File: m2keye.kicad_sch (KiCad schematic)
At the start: 17 parts

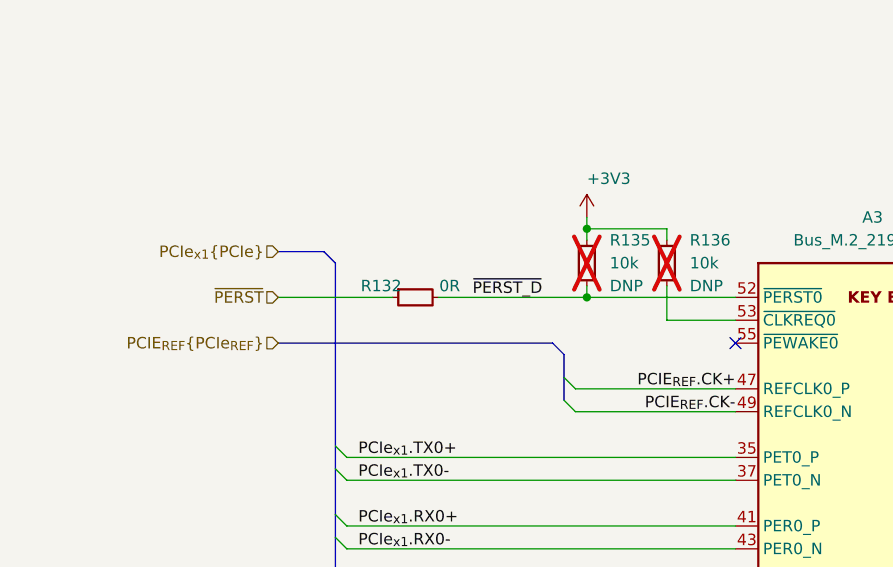
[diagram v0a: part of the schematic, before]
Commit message: [#58904] Change pinout of backplane connector. Connect CLKREQ from PCIe devices
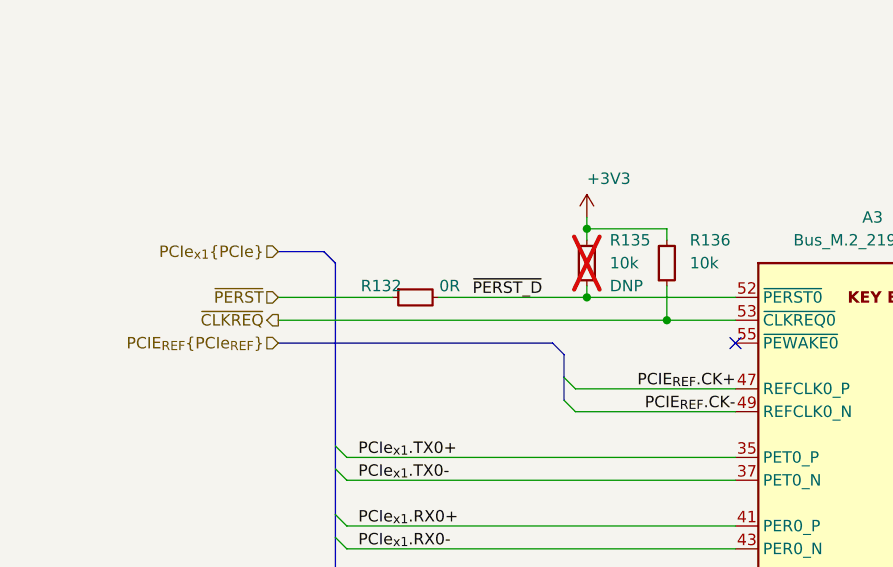
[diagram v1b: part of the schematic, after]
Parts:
- R136: DNP DNP -> (none); now fitted
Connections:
- net ~{CLKREQ}: now reaches A3.53 (~{CLKREQ0}), R136.1
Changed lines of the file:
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@@
   (junction (at 166.37 82.55) (diameter 0) (color 0 0 0 0)
+  )
+  (junction (at 175.26 85.09) (diameter 0) (color 0 0 0 0)
   )
   (junction (at 218.44 189.23) (diameter 0) (color 0 0 0 0)
@@
     (stroke (width 0) (type default))
   )
+  (wire (pts (xy 132.08 85.09) (xy 175.26 85.09))
+    (stroke (width 0) (type default))
+  )
   (bus (pts (xy 138.43 158.75) (xy 138.43 161.29))
     (stroke (width 0) (type default))
@@
   )
   (hierarchical_label "PCIe_{x1}{PCIe}" (shape input) (at 132.08 77.47 180) (fields_autoplaced)
+    (effects (font (size 1.27 1.27)) (justify right))
+  )
+  (hierarchical_label "~{CLKREQ}" (shape output) (at 132.08 85.09 180) (fields_autoplaced)
     (effects (font (size 1.27 1.27)) (justify right))
   )
@@
   )
   (symbol (lib_id "antmicroResistors0402:R_10k_0402") (at 175.26 81.28 90) (unit 1)
-    (in_bom yes) (on_board yes) (dnp yes) (fields_autoplaced)
+    (in_bom yes) (on_board yes) (dnp no) (fields_autoplaced)
     (property "Reference" "R136" (at 177.8 76.2 90)
       (effects (font (size 1.27 1.27) (thickness 0.15)) (justify right))
@@
       (effects (font (size 1.27 1.27)) (justify left bottom) hide)
     )
-    (property "DNP" "DNP" (at 177.8 81.28 90)
-      (effects (font (size 1.27 1.27)) (justify right))
-    )
     (pin "2")

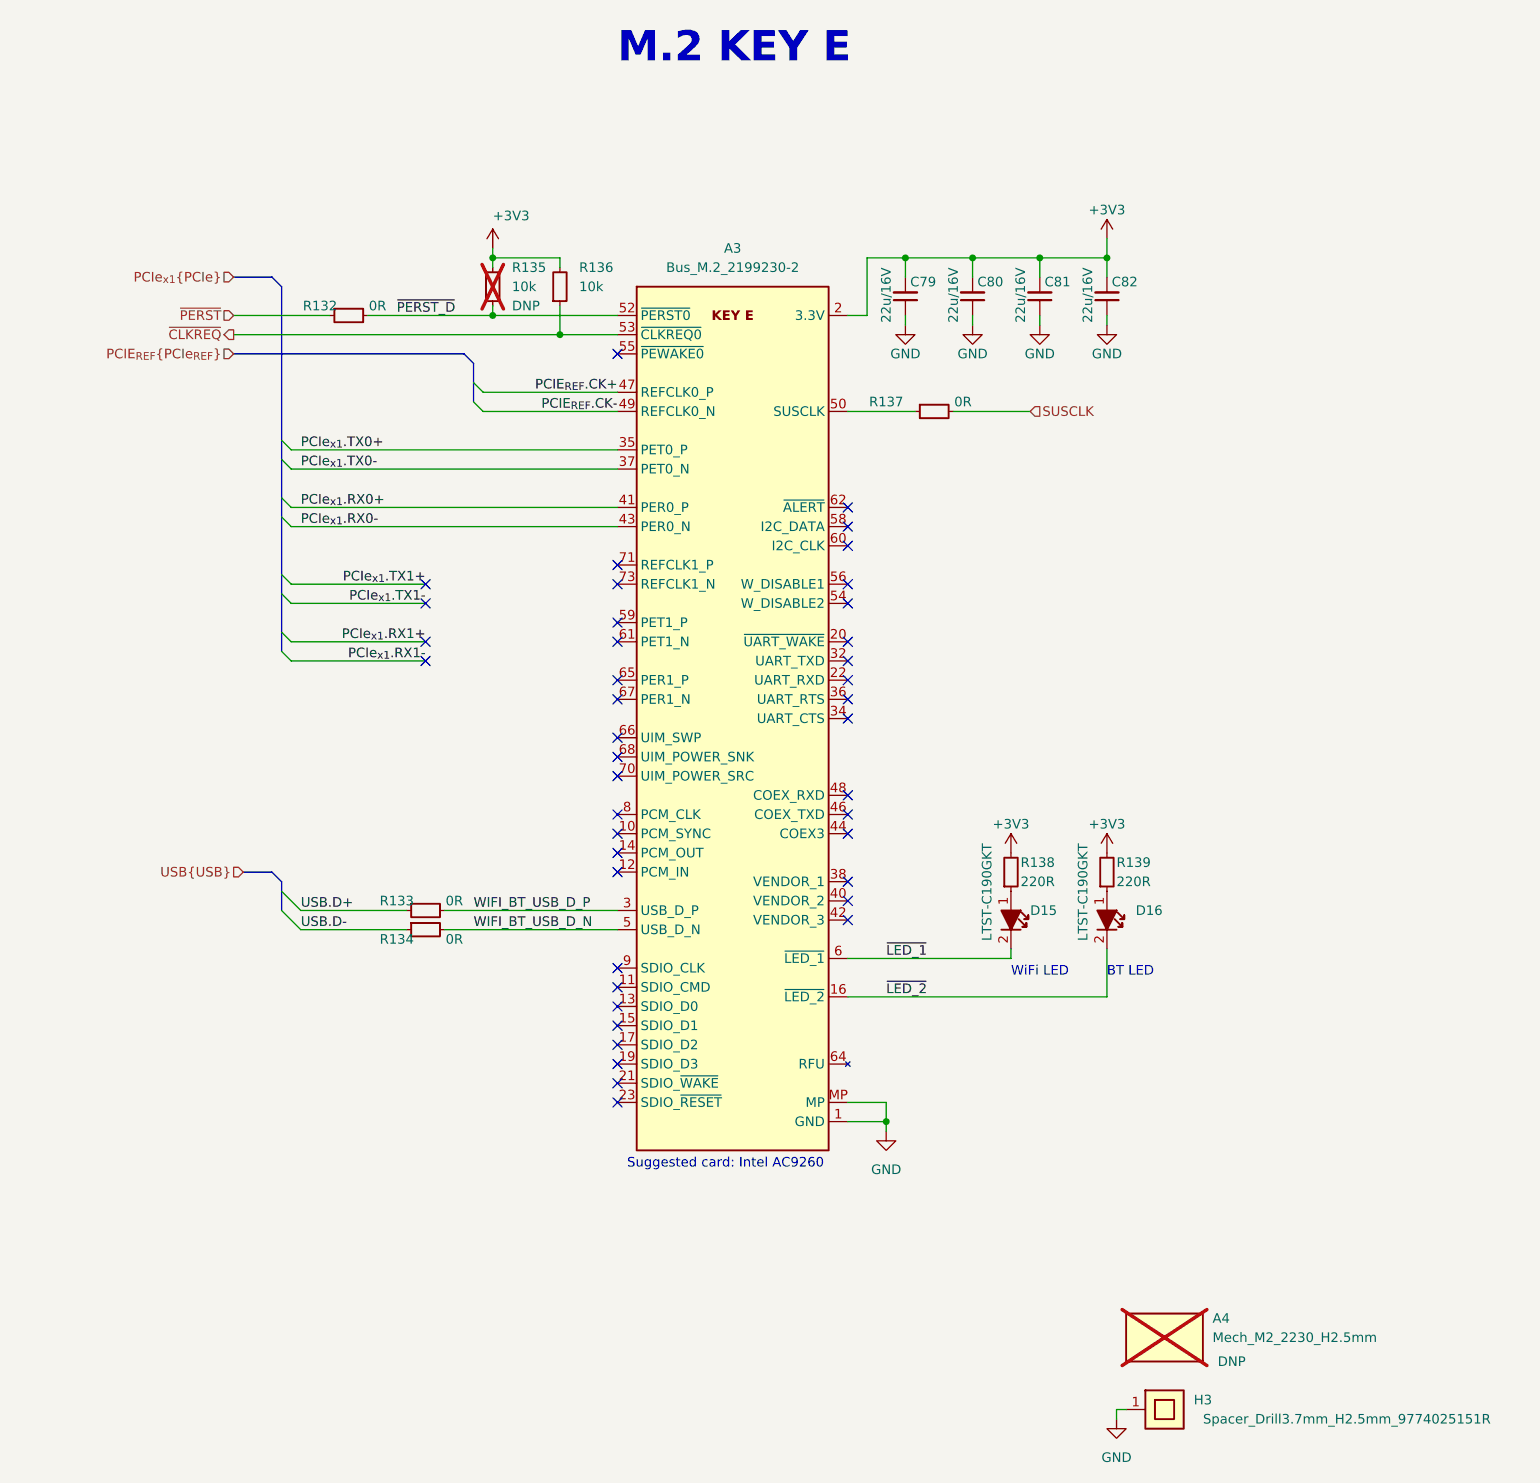
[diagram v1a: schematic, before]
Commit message: Update components from the library
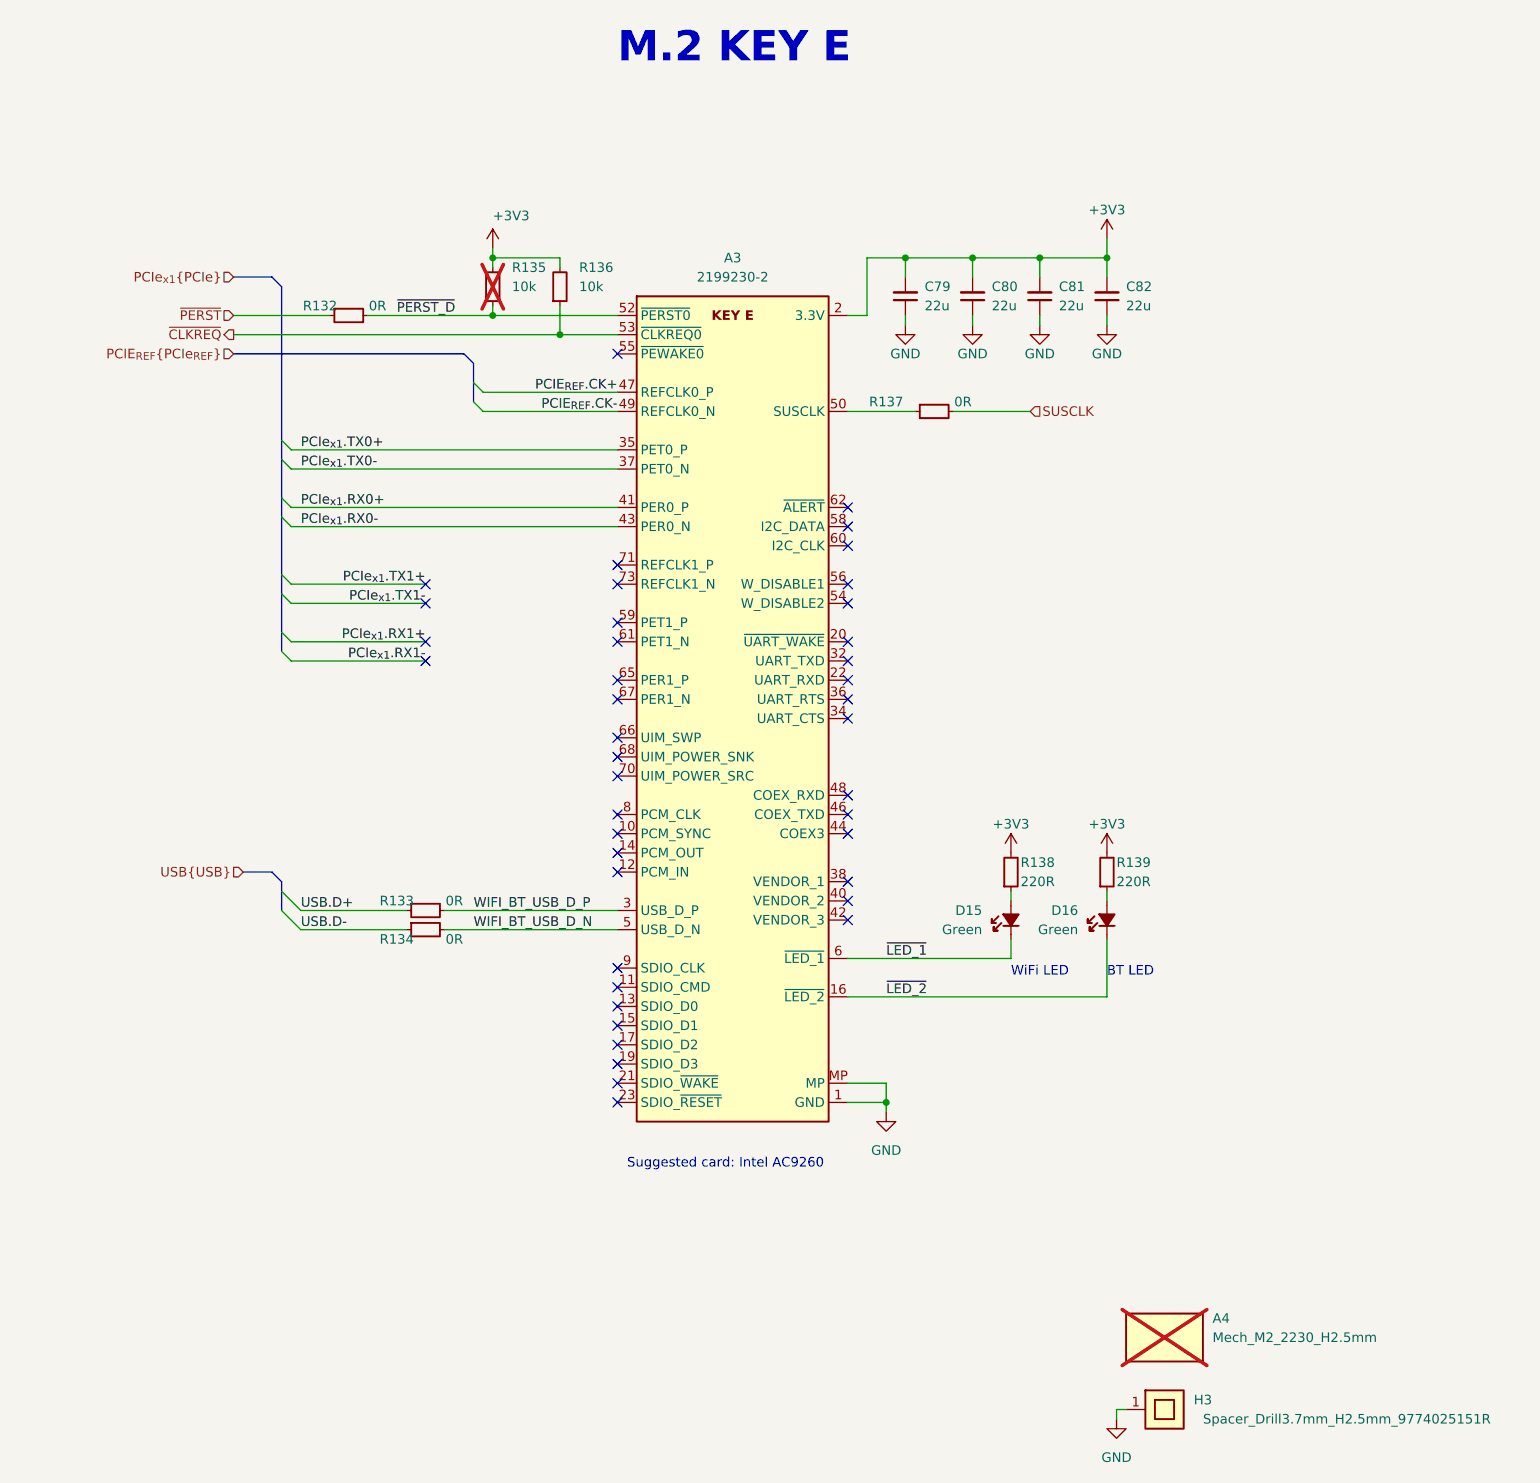
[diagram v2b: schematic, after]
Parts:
- A3: VSD_Class M.2 Key E -> (none)
- A4: Author (none) -> Antmicro; Copyright Copyright (c) 2023 Antmicro -> (none); DNP DNP -> (none); License Apache-2.0 License -> Apache-2.0; Public (none) -> False
- C79, C80, C81, C82: Public (none) -> False; Val 22u/16V -> 22u; Voltage (none) -> 16V
- D15, D16: Color (none) -> Green; Manufacturer Lite-On Inc. -> Lite-On; Public (none) -> False
- H3, R132, R136: Public (none) -> False
- R133, R134, R137, R138, R139: Copyright Copyright (c) 2023 Antmicro -> (none); Public (none) -> False
- R135: DNP DNP -> (none); Public (none) -> False
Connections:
- net ~{LED_1}: now also D15.1 (C); no longer D15.2
- net ~{LED_2}: now also D16.1 (C); no longer D16.2
- net at R138.1: now also D15.2 (A); no longer D15.1
- net at R139.1: now also D16.2 (A); no longer D16.1
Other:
- moved on the sheet: D15, D16

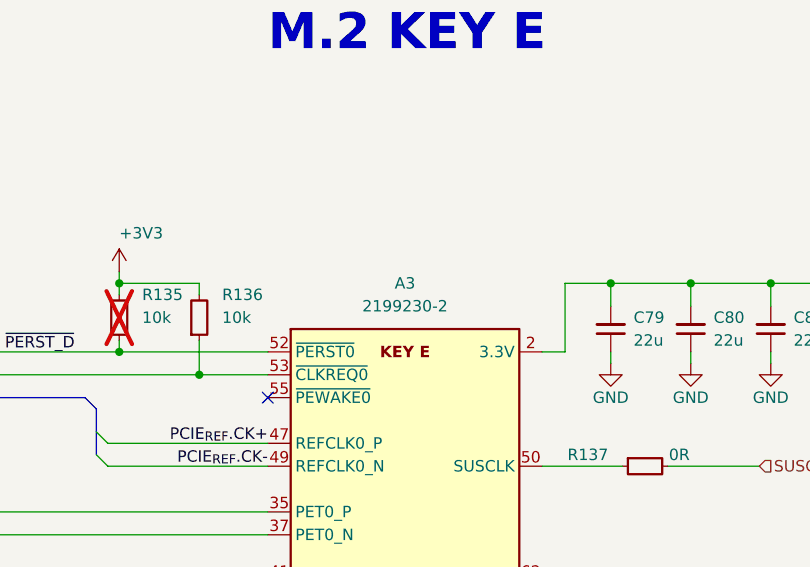
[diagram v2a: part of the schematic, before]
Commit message: Fix component visualization issues
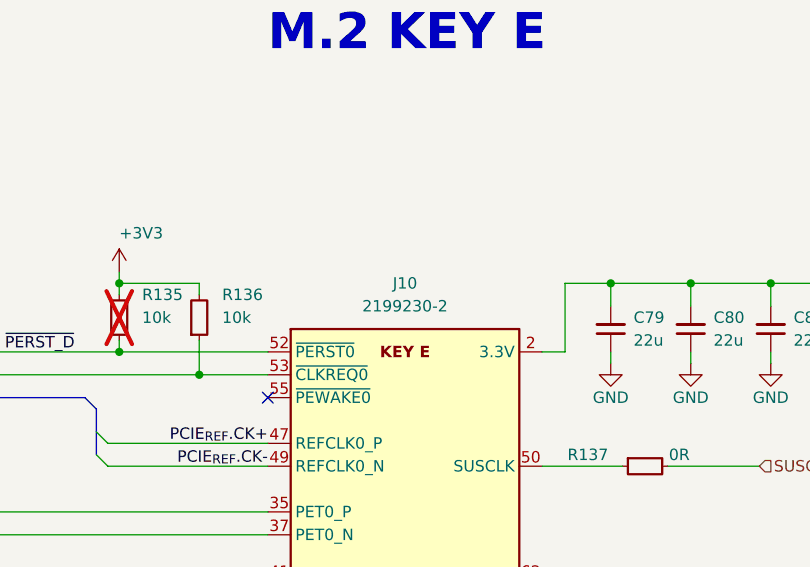
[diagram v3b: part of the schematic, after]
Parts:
- renumbered A3 to J10
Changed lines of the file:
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@@
   (symbol (lib_id "antmicroPciConnectors:Bus_M.2_2199230-2") (at 182.88 82.55 0) (unit 1)
     (in_bom yes) (on_board yes) (dnp no) (fields_autoplaced)
-    (property "Reference" "A3" (at 198.12 74.93 0)
+    (property "Reference" "J10" (at 198.12 74.93 0)
       (effects (font (size 1.27 1.27) (thickness 0.15)))
     )
@@
       (project "com-express-7-baseboard"
         (path "/1b8c34da-dad5-4b0b-8c4b-45db766c4dfa/ebb6e8c2-9d30-49b6-83d5-1732977f9e4c"
-          (reference "A3") (unit 1)
+          (reference "J10") (unit 1)
         )
       )

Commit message: Add Mech_SolidRun_LX2160A-CEX7 to schematic
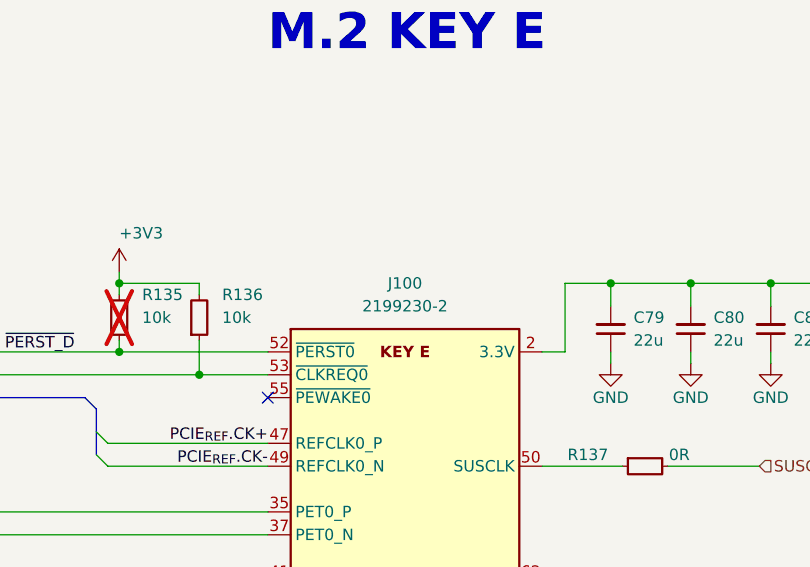
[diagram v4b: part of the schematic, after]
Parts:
- renumbered J10 to J100
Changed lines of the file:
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@@
   (symbol (lib_id "antmicroPciConnectors:Bus_M.2_2199230-2") (at 182.88 82.55 0) (unit 1)
     (in_bom yes) (on_board yes) (dnp no) (fields_autoplaced)
-    (property "Reference" "J10" (at 198.12 74.93 0)
+    (property "Reference" "J100" (at 198.12 74.93 0)
       (effects (font (size 1.27 1.27) (thickness 0.15)))
     )
@@
       (project "com-express-7-baseboard"
         (path "/1b8c34da-dad5-4b0b-8c4b-45db766c4dfa/ebb6e8c2-9d30-49b6-83d5-1732977f9e4c"
-          (reference "J10") (unit 1)
+          (reference "J100") (unit 1)
         )
       )

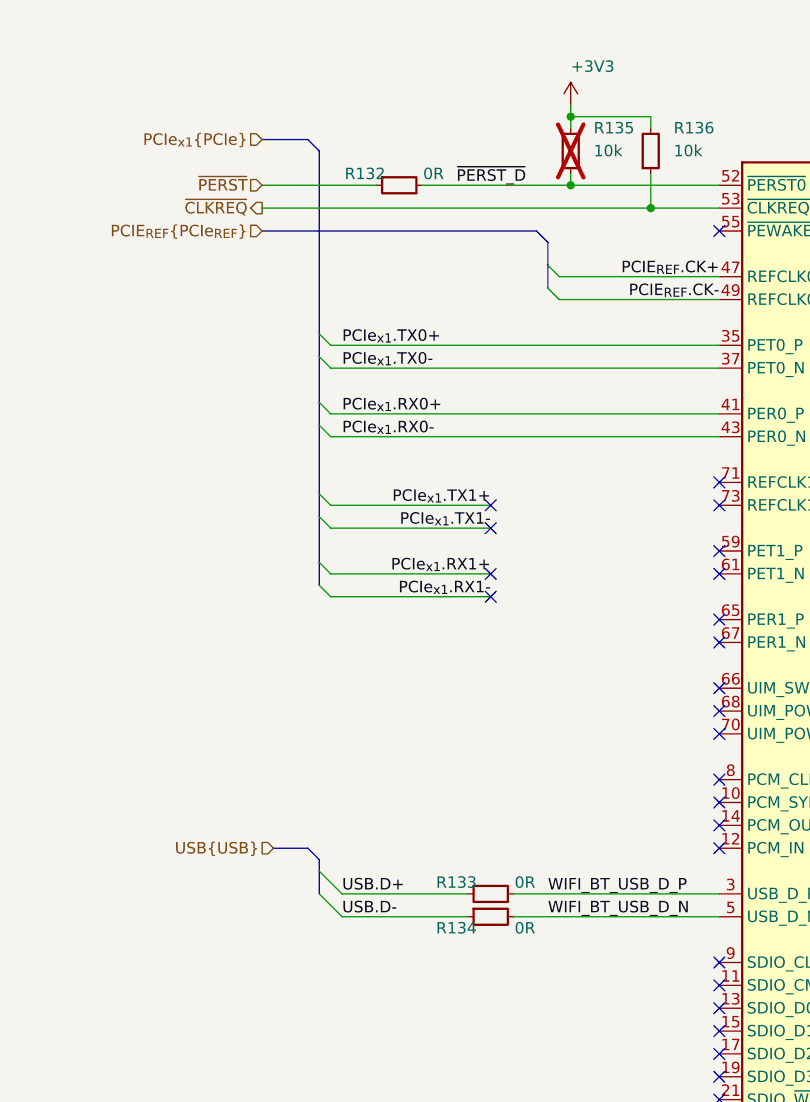
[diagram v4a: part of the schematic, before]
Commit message: [#65447] Fix rotated LEDs, overlapping text and symbols, add rules
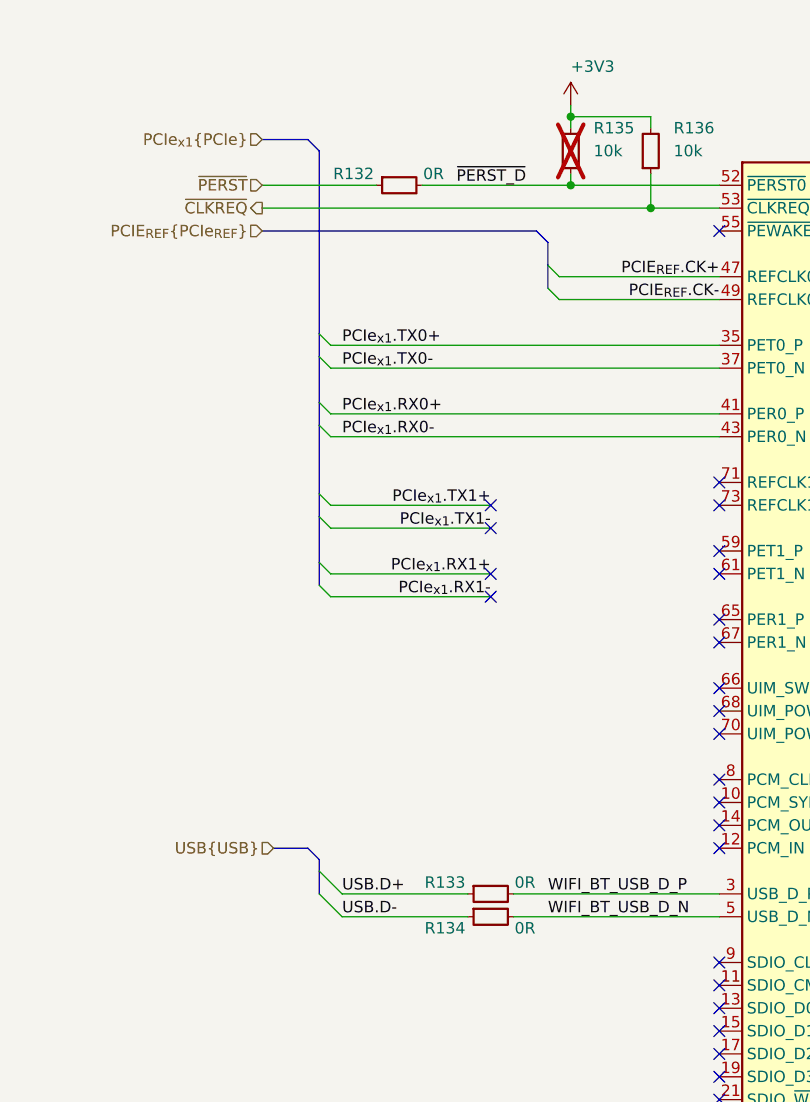
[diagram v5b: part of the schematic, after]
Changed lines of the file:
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@@
   (symbol (lib_id "antmicroResistors0402:R_0R_0402") (at 154.94 161.29 0) (unit 1)
     (in_bom yes) (on_board yes) (dnp no)
-    (property "Reference" "R133" (at 153.67 160.02 0)
+    (property "Reference" "R133" (at 152.4 160.02 0)
       (effects (font (size 1.27 1.27) (thickness 0.15)))
     )
@@
   (symbol (lib_id "antmicroResistors0402:R_0R_0402") (at 144.78 82.55 0) (unit 1)
     (in_bom yes) (on_board yes) (dnp no)
-    (property "Reference" "R132" (at 143.51 81.28 0)
+    (property "Reference" "R132" (at 142.24 81.28 0)
       (effects (font (size 1.27 1.27) (thickness 0.15)))
     )
@@
   (symbol (lib_id "antmicroResistors0402:R_0R_0402") (at 154.94 163.83 0) (unit 1)
     (in_bom yes) (on_board yes) (dnp no)
-    (property "Reference" "R134" (at 153.67 165.1 0)
+    (property "Reference" "R134" (at 152.4 165.1 0)
       (effects (font (size 1.27 1.27) (thickness 0.15)))
     )
